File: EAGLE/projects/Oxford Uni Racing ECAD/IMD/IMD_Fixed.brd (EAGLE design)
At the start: 160 x 100 mm, 13 parts, among them IC1 LM2901N, IC2 555, K1 RT444012, X1 Connector i

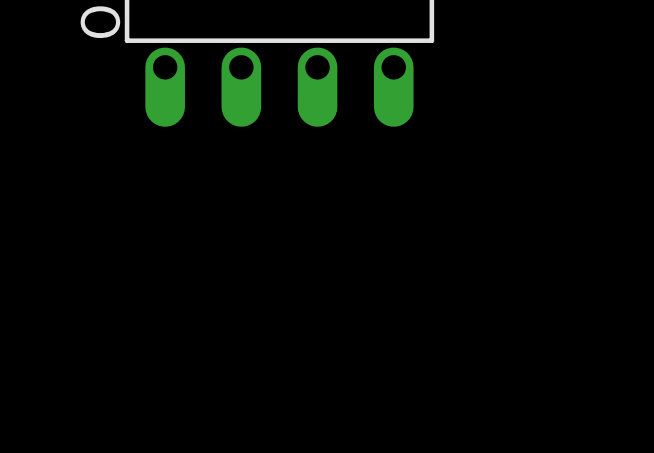
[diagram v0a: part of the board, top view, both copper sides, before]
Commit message: added decoupling capacitors
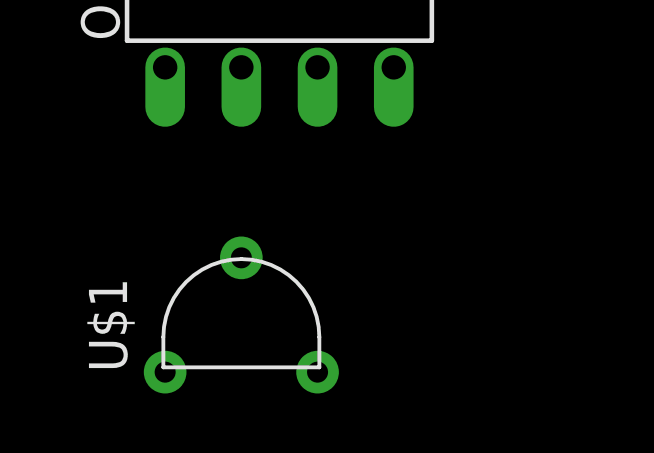
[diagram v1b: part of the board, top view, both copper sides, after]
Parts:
- added U$1: (no value), v-reg_supertex:N3
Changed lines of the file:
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@@
 <attribute name="VALUE" x="-46.736" y="-46.355" size="1.27" layer="27" ratio="10"/>
+</element>
+<element name="U$1" library="v-reg_supertex" package="N3" value="" x="-44.45" y="-58.42" smashed="yes">
+<attribute name="NAME" x="-48.26" y="-59.69" size="1.27" layer="25" rot="R90"/>
+<attribute name="VALUE" x="-39.37" y="-59.69" size="1.27" layer="27" rot="R90"/>
 </element>
 </elements>

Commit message: done schematics on IMD
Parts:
- added C1: 1uF, adafruit:C050-024X044
- added C2: 15uF, adafruit:C050-024X044
- added C4: 10uF, adafruit:C050-024X044
- added C5: 10nF, adafruit:C050-024X044
- added R10, R9: 330, adafruit:0204/7
- added R11, R12, R16: 10K, adafruit:M0805
- added R13: 12K, adafruit:M0805
- added R14, R5: 4.7K, adafruit:M0805
- added R15, R6, R7: 330, adafruit:M0805
- added R3: 1K, adafruit:M0805
- added R4: 6.8K, adafruit:M0805
- added R8: 1K, adafruit:0204/7
- added RED_LIGHT_TR, TIMER_TR: IRLML2502GTRPBF, adafruit:SOT23
- added T1: IRLML6402, zetex:SOT-23
- added X2: GREEN_LIGHTS, con-wago-500:W237-102
- added X3: RED_LIGHTS, con-wago-500:W237-102
- F1: value 1A -> 3-5A
- U$1: value (none) -> LR8N3
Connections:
- removed net VCC+: IC2.8
- new net GREEN_LIGHT_OUT+: T1.2, X2.2
- new net HV+: D2.C
- new net HV-: C1.2, OK1.3, R9.1
- new net N$10: C2.1, OK1.6, R3.1, R4.2, R6.1, R7.1
- new net N$11: R12.1, R6.2, T1.3
- new net N$12: R11.2, R7.2, TIMER_TR.1
- new net N$13: C4.2, C5.2, IC2.1, TIMER_TR.3
- new net N$14: R15.2, R16.2, RED_LIGHT_TR.1
- new net N$15: IC2.7, R13.2, R14.1
- new net N$16: C4.1, IC2.2, IC2.6, R13.1
- new net N$17: C5.1, IC2.5
- new net N$18: IC2.3, R15.1
- new net N$5: D2.A, U$1.1
- new net N$7: R8.1, R9.2, U$1.3
- new net N$8: OK1.2, R10.1
- new net N$9: C1.1, R10.2, R8.2, U$1.2
- new net RED_LIGHT_OUT-: RED_LIGHT_TR.3, X3.1
- new net VCU_OUT: J2.2, R4.1, R5.2
- net 12V: now also IC2.4, IC2.8, OK1.8, R12.2, R14.2, R3.2, T1.1, X3.2
- net GND: now also C2.2, J2.1, J2.3, J2.5, OK1.5, R11.1, R16.1, R5.1, RED_LIGHT_TR.2, TIMER_TR.2, X2.1; no longer IC2.1, J2.7
- net IMD_REF: now also J2.4; no longer J2.6
- net N$2: now also J2.6, J2.7

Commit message: routed IMD
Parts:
- added C3: 0.1uF, adafruit:C050-024X044
- moved X3 352.2 mm to (148.6, 81.3), turned to 90 degrees
- moved R16 341.0 mm to (139.7, 91.4), flipped to the bottom, turned to 180 degrees
- moved R15 331.5 mm to (139.7, 86.4), flipped to the bottom, turned to 180 degrees
- moved X2 328.2 mm to (148.6, 64.8), turned to 90 degrees
- moved R14 318.0 mm to (116.8, 91.4), flipped to the bottom, turned to 180 degrees
- moved R13 306.3 mm to (113.0, 86.4), flipped to the bottom, turned to 90 degrees
- moved C5 300.5 mm to (132.1, 73.7), turned to 270 degrees
- moved C4 287.4 mm to (113.0, 78.7), turned to 270 degrees
- moved RED_LIGHT_TR 286.0 mm to (142.2, 80.0), flipped to the bottom, turned to 180 degrees
- moved R12 281.3 mm to (132.1, 62.2), flipped to the bottom, turned to 180 degrees
- moved T1 279.6 mm to (139.7, 64.8), flipped to the bottom, turned to 90 degrees
- moved R11 267.5 mm to (113.0, 66.0), flipped to the bottom, turned to 90 degrees
- moved TIMER_TR 254.7 mm to (111.8, 72.4), flipped to the bottom
- moved R6 223.9 mm to (125.7, 62.2), flipped to the bottom, turned to 180 degrees
- moved R7 217.4 mm to (109.2, 66.0), flipped to the bottom, turned to 90 degrees
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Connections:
- net 12V: now also C3.1
- net GND: now also C3.2
- net IMD_REF: now also J2.2; no longer J2.4
- net VCU_OUT: now also J2.4; no longer J2.2
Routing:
- net 12V: track 0.00 -> 296.1 mm, vias 0 -> 4
- net IMD_REF: track 0.00 -> 102.3 mm
- net VCU_OUT: track 0.00 -> 62.1 mm
- net GND: track 0.00 -> 61.7 mm, vias 0 -> 6
- net N$10: track 0.00 -> 53.2 mm
- net N$1: track 0.00 -> 38.3 mm
- net N$13: track 0.00 -> 38.0 mm, vias 0 -> 2
- net N$18: track 0.00 -> 31.9 mm
- net HV-: track 0.00 -> 29.7 mm
- net N$15: track 0.00 -> 24.0 mm
- net N$8: track 0.00 -> 23.0 mm
- net ASS1: track 0.00 -> 21.9 mm
- net ASS2: track 0.00 -> 21.8 mm
- net N$16: track 0.00 -> 20.8 mm
- net N$2: track 0.00 -> 19.0 mm
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- added copper zone on layer 16, net GND
